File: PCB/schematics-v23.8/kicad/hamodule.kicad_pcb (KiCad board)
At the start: 2 copper layers, 129.2 x 84.3 mm, 146 parts, among them J1 GND|5V, J10 Tx|Rx, J11 USB_C_Receptacle_USB2.0, J12 2604-1104, J14 2604-1104, J15 2604-1104, J2 2604-1102, J3 Sda|Scl, J4 13|12, J5 9|3|16, J6 GND|3.3V, J7 Conn_01x02_Pin, J9 2604-1104, K1 AQG12205, K2 AQG12205, K3 AQG12205, K4 AQG12205, K5 AQG12205, K6 AQG12205, K7 AQG12205, K8 AQG12205, SW1 Reset, SW2 Boot, SW3 USB | PS, U1 LD1117AV33, U10 ULN2803A, U2 ESP32-S3-WROOM-2, U3 LDA210-PDIP, U4 USBLC6-2SC6, U5 LDA210-PDIP, U6 LDA210-PDIP, U7 SHT4x, U8 LDA210-PDIP, U9 MCP23017_SO

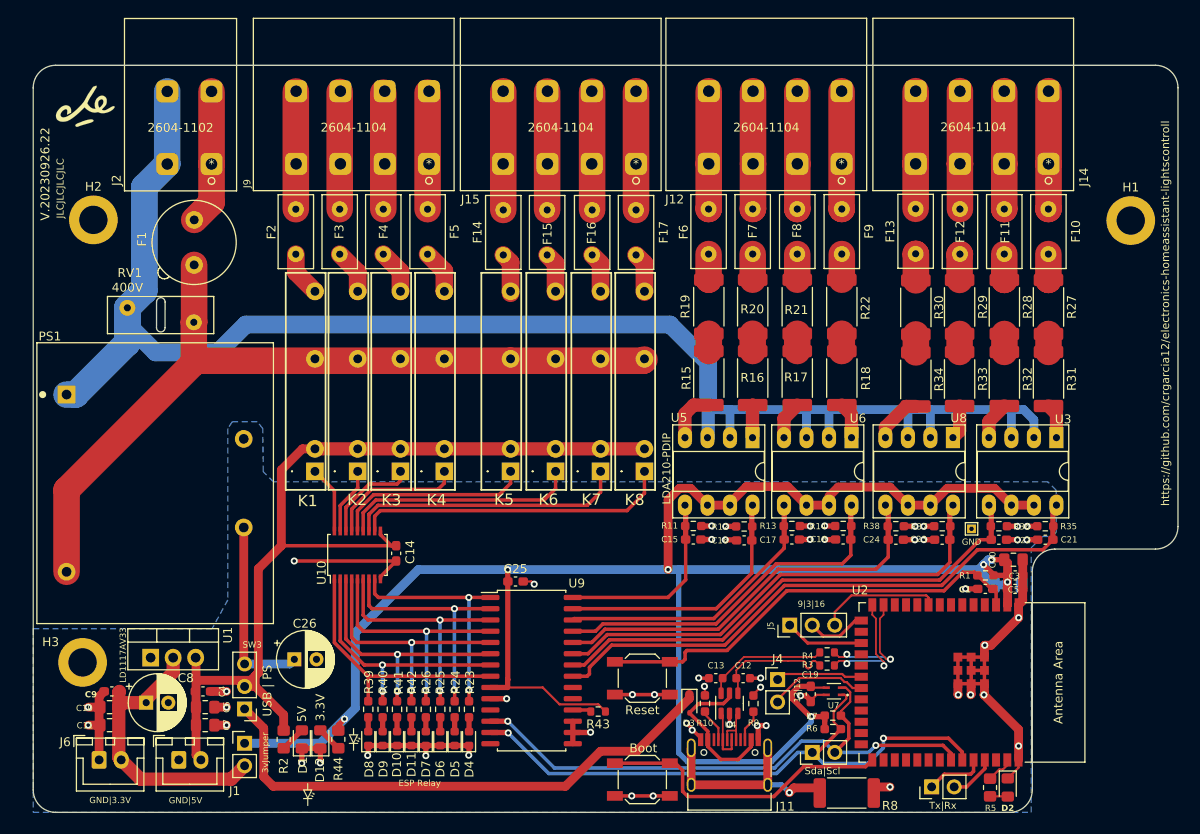
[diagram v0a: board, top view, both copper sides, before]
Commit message: [V23.8] Adding screen connector + Fixing version + adding caps
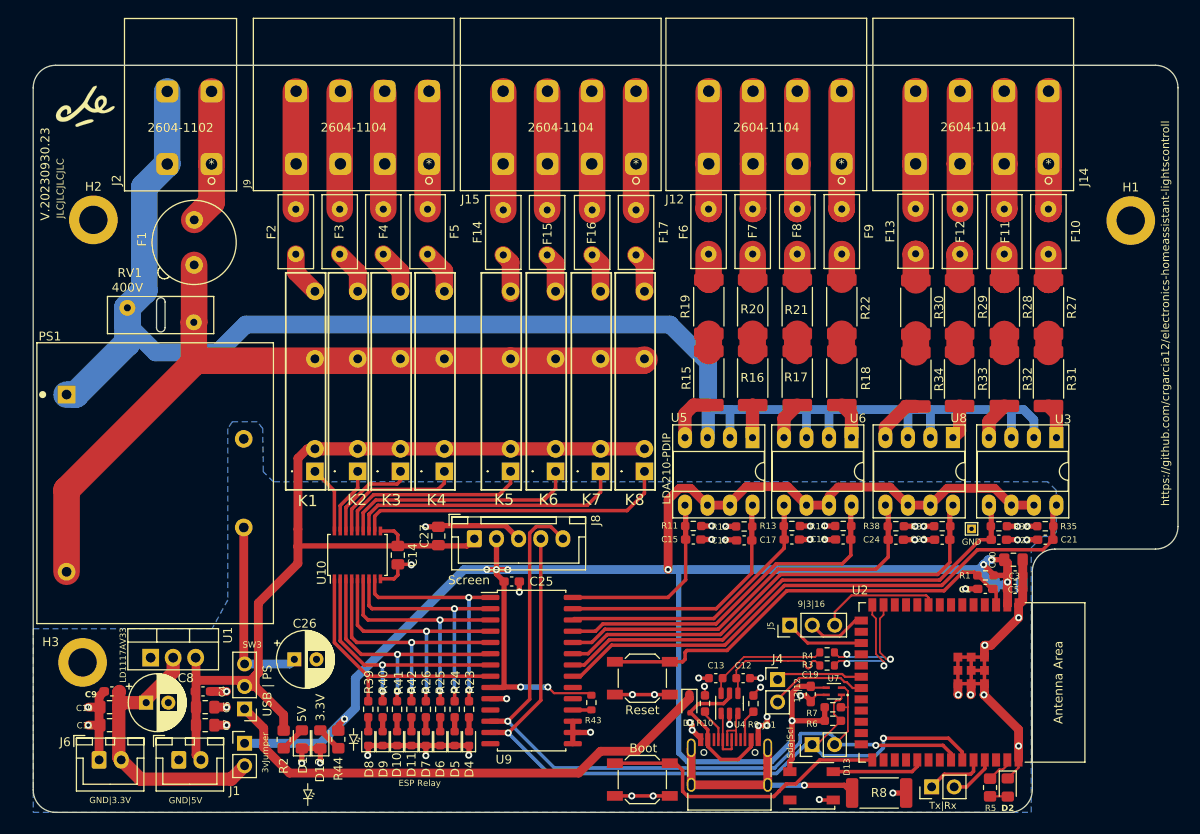
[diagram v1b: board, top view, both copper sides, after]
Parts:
- added C27: 22uF, Capacitor_SMD:C_0805_2012Metric_Pad1.18x1.45mm_HandSolder, F.Cu at (69.6, 85.3)
- added D13: Inolux_IN-PI554FCH, LED_SMD:LED_Inolux_IN-PI554FCH_PLCC4_5.0x5.0mm_P3.2mm, F.Cu at (111.7, 113.5)
- added J8: Screen, Connector_JST:JST_XH_B5B-XH-A_1x05_P2.50mm_Vertical, F.Cu at (73.7, 85.6)
- C14: footprint Capacitor_SMD:C_0603_1608Metric_Pad1.08x0.95mm_HandSolder -> Capacitor_SMD:C_0805_2012Metric_Pad1.18x1.45mm_HandSolder
- moved R8 3.66 mm to (119.4, 114.4)
- moved R43 1.27 mm to (86.9, 104.1), turned to -90 degrees
- moved R6 0.94 mm to (114.1, 106.2)
- moved R7 0.94 mm to (114.1, 104.7)
- moved J3 0.88 mm to (111.8, 108.9)
- moved C25 0.43 mm to (77.9, 90.5)
- moved C14 0.28 mm to (65.0, 87.5)
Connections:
- U2 pad 31: unconnected-(U2-GPIO38/FSPIWP/SUBSPIWP-Pad31) -> RGBLED
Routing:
- net SCL: track 68.3 -> 93.7 mm
- net SDA: track 69.6 -> 91.7 mm
- net RGBLED: track 0.00 -> 10.5 mm
- net 5V+: track 112.0 -> 119.7 mm
- net 3.3V+: track 246.2 -> 253.1 mm, vias 7 -> 11
- net GND: track 152.0 -> 155.5 mm, vias 52 -> 55
- net VBUS: track 61.6 -> 58.4 mm
- net Net-(J11-SHIELD): track 24.2 -> 26.9 mm
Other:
- board text added: "V.20230930.23"
- board text removed: "V.20230926.22"

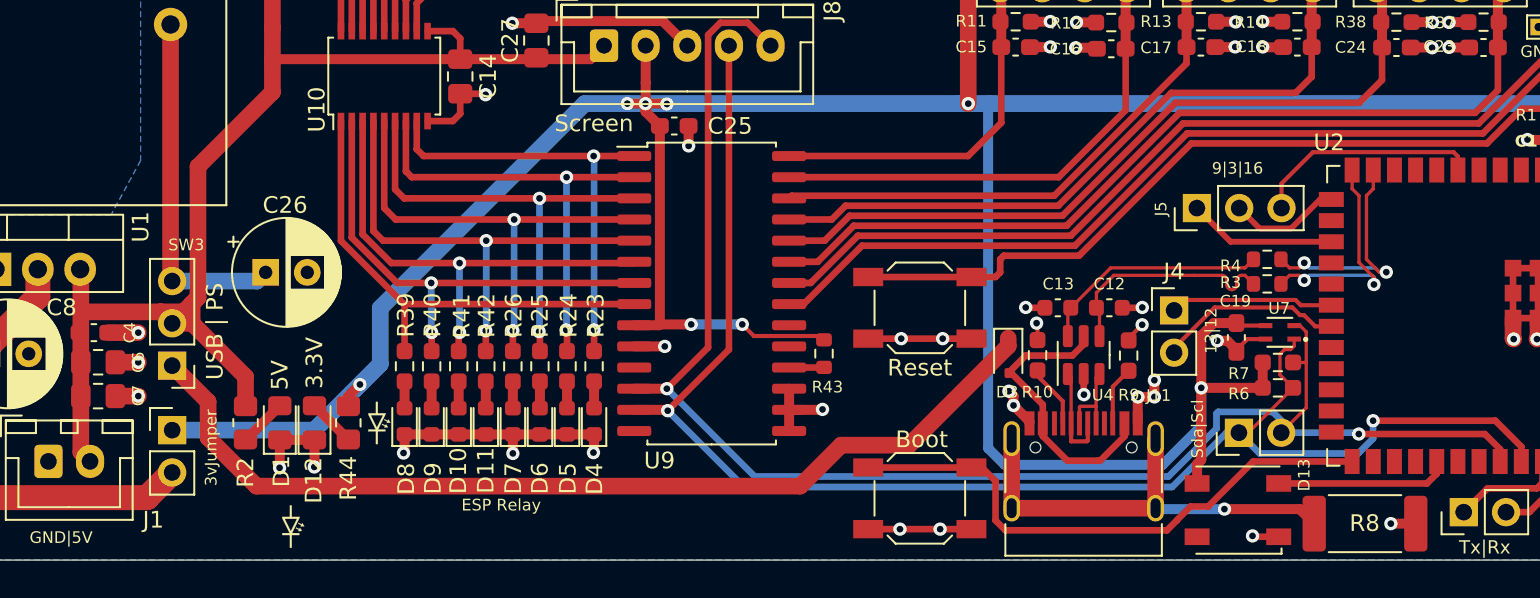
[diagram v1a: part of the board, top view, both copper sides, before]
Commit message: adding RGB Led
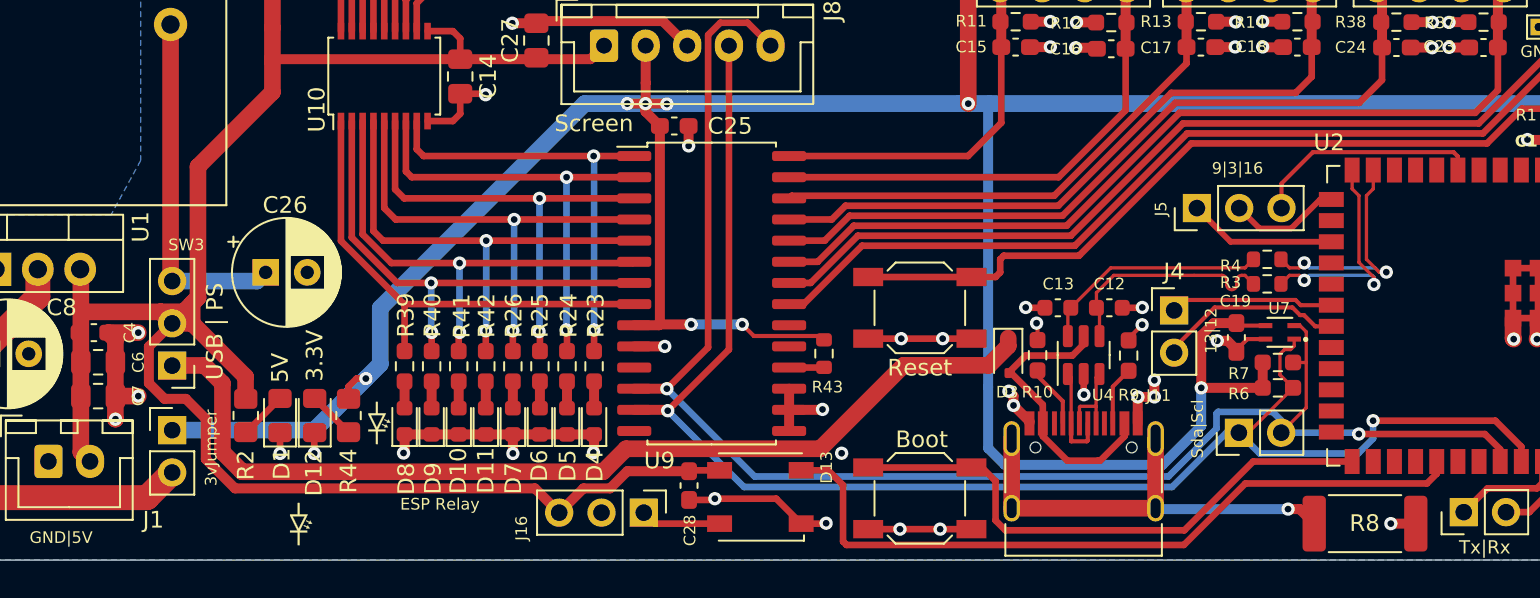
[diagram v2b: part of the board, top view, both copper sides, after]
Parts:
- added C28: 100nF, Capacitor_SMD:C_0603_1608Metric_Pad1.08x0.95mm_HandSolder, F.Cu at (78.8, 112.1)
- added J16: 9|3|16, Connector_PinHeader_2.54mm:PinHeader_1x03_P2.54mm_Vertical, F.Cu at (76.1, 113.7)
- moved D13 28.7 mm to (83.1, 112.8)
- moved G4 0.49 mm to (55.5, 114.4)
- moved D1 0.44 mm to (54.2, 107.9)
- moved D12 0.44 mm to (56.3, 107.9)
- moved R2 0.44 mm to (52.2, 107.9)
- moved R44 0.44 mm to (58.3, 107.9)
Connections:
- D13 pad 3: 3.3V+ -> 5V+
- D13 pad 4: unconnected-(D13-DO-Pad4) -> Net-(D13-DO)
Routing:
- net 5V+: track 119.7 -> 163.4 mm
- net RGBLED: track 10.5 -> 44.5 mm
- net GND: track 155.5 -> 163.9 mm, vias 55 -> 57
- net 3.3V+: track 253.1 -> 247.7 mm
- net Net-(D13-DO): track 0.00 -> 4.82 mm

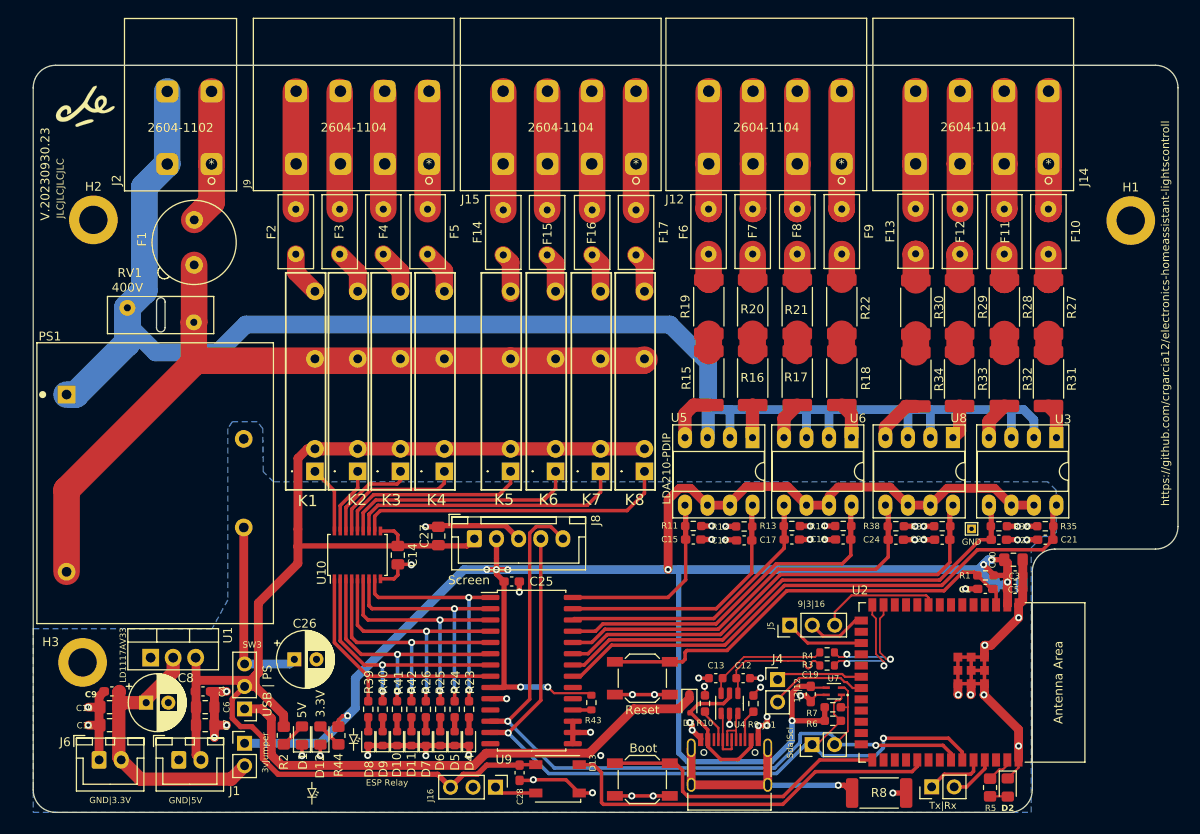
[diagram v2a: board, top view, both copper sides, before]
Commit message: [23.8] Adding RGB Led, fixing placing and silkscreen
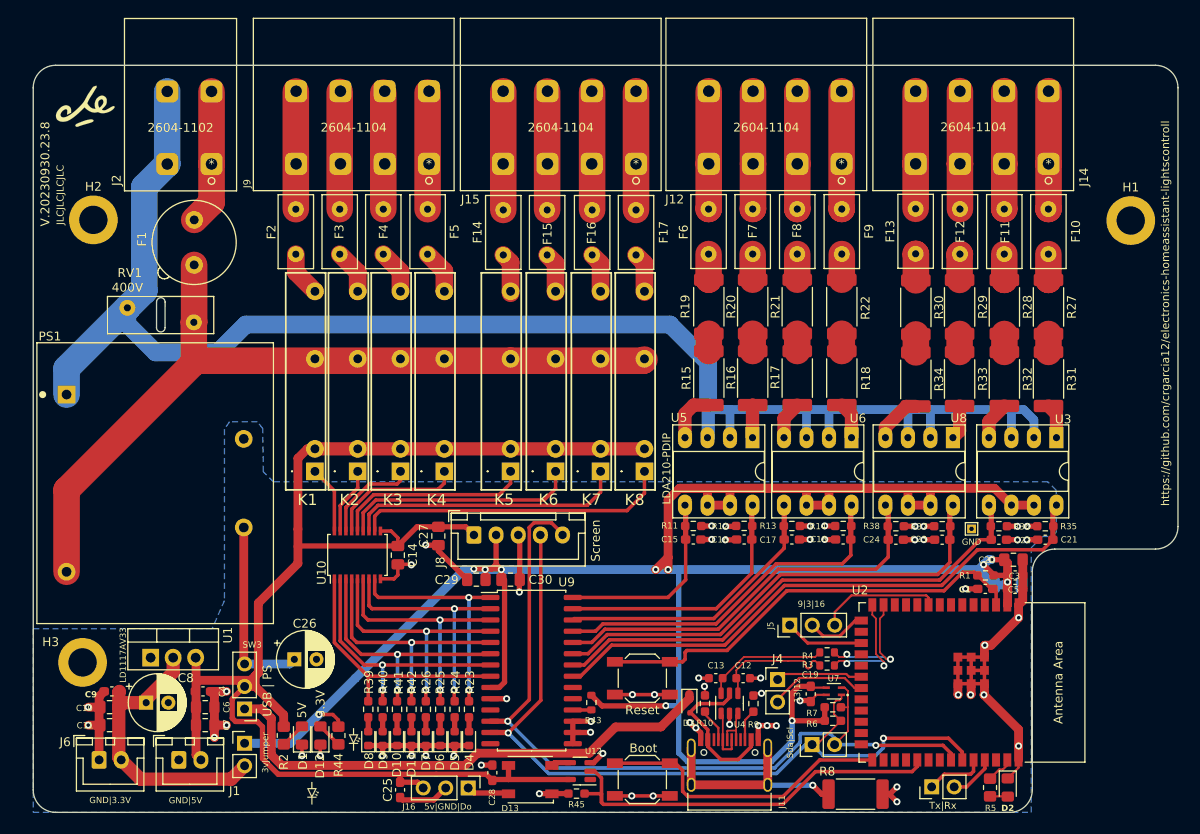
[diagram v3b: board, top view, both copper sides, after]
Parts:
- added C29: 100nF, Capacitor_SMD:C_0805_2012Metric_Pad1.18x1.45mm_HandSolder, F.Cu at (73.9, 90.3)
- added C30: 100nF, Capacitor_SMD:C_0805_2012Metric_Pad1.18x1.45mm_HandSolder, F.Cu at (77.8, 90.3)
- added R45: 10kΩ, Resistor_SMD:R_0603_1608Metric_Pad0.98x0.95mm_HandSolder, F.Cu at (85.2, 114.4)
- added U12: SN74LV1T34DBV, Package_TO_SOT_SMD:SOT-23-5, F.Cu at (85.6, 111.9)
- C27: value 22uF -> 100nF
- J16: value 9|3|16 -> 5v|GND|Do
- moved C25 26.7 mm to (65.3, 114.0), turned to -90 degrees
- moved D13 3.08 mm to (80.0, 112.8)
- moved J16 3.08 mm to (73.0, 113.8)
- moved C28 3.08 mm to (75.7, 112.1), turned to 90 degrees
- moved R8 2.67 mm to (116.7, 114.5)
- moved J8 0.43 mm to (73.6, 85.2)
- moved C16 0.10 mm to (104.1, 85.7)
- moved R12 0.06 mm to (104.1, 84.2)
- turned C27 to -90 degrees
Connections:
- C25 pad 1: 3.3V+ -> 5V+
- D13 pad 2: RGBLED -> Net-(D13-DIN)
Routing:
- net 3.3V+: track 247.7 -> 295.3 mm
- net GND: track 163.9 -> 173.3 mm, vias 57 -> 60
- net 5V+: track 163.4 -> 172.5 mm
- net Net-(J11-SHIELD): track 26.9 -> 24.3 mm
- net Net-(D13-DIN): track 0.00 -> 2.18 mm
- net RGBLED: track 44.5 -> 45.5 mm
- net SCL: track 93.7 -> 94.3 mm
- net 220VAC(N): track 111.3 -> 110.7 mm
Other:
- board text added: "V.20230930.23.8"
- board text removed: "ESP Relay"
- board text removed: "V.20230930.23"

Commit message: setting up for a new case
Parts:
- added G***: LOGO, icons:qr_code_m, B.Cu at (84.5, 104.4)
- moved G3 85.0 mm to (35.3, 78.4)
- moved G1 21.5 mm to (26.8, 58.1), turned to 90 degrees
- moved H2 14.1 mm to (27.0, 36.0)
- moved H1 14.0 mm to (150.3, 36.0)
- moved H3 10.6 mm to (27.0, 109.9)
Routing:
- net 3.3V+: track 295.3 -> 245.3 mm, vias 11 -> 7
- net GND: track 173.3 -> 211.3 mm, vias 60 -> 68
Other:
- board size 129.2 x 84.3 mm -> 129.6 x 84.3 mm
- board text added: "locked"
- board text removed: "JLCJLCJLCJLC"
- board text removed: "V.20230930.23.8"

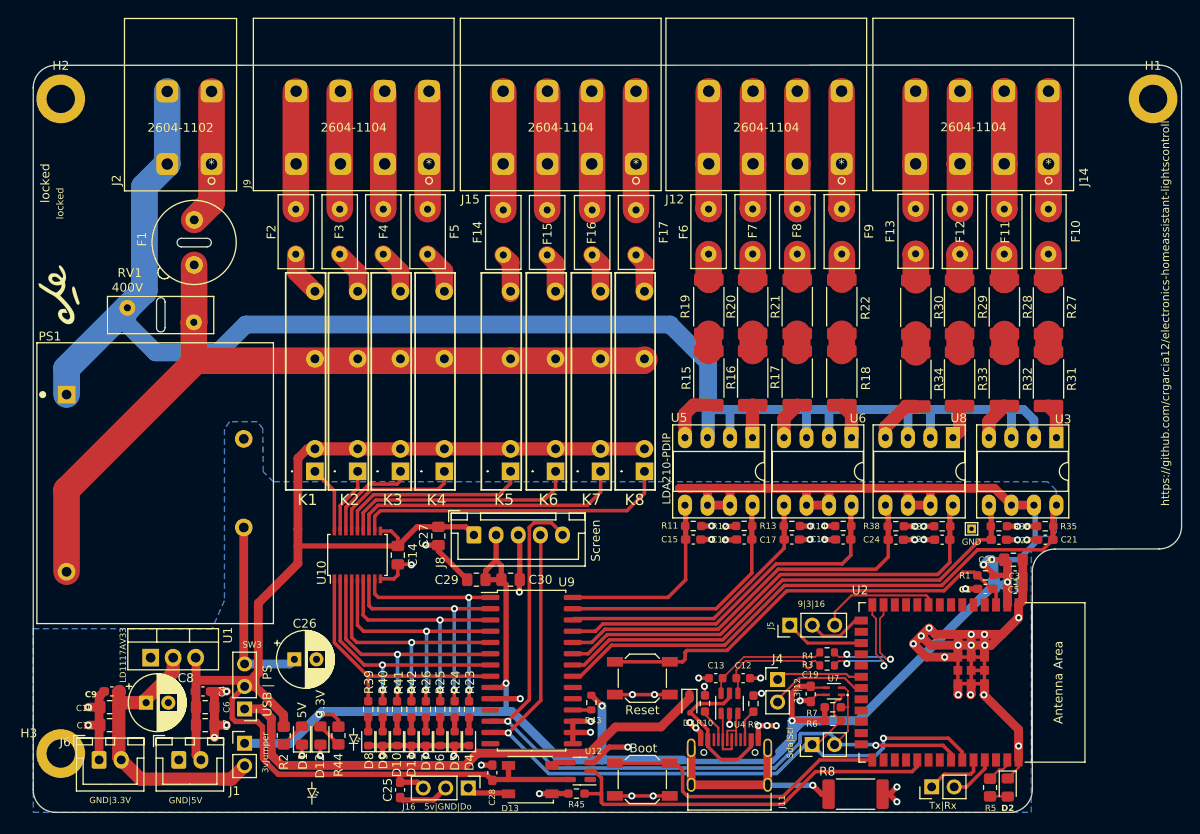
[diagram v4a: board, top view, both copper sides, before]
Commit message: fixing power sockets (3.3v and 5v) + prod files + readme
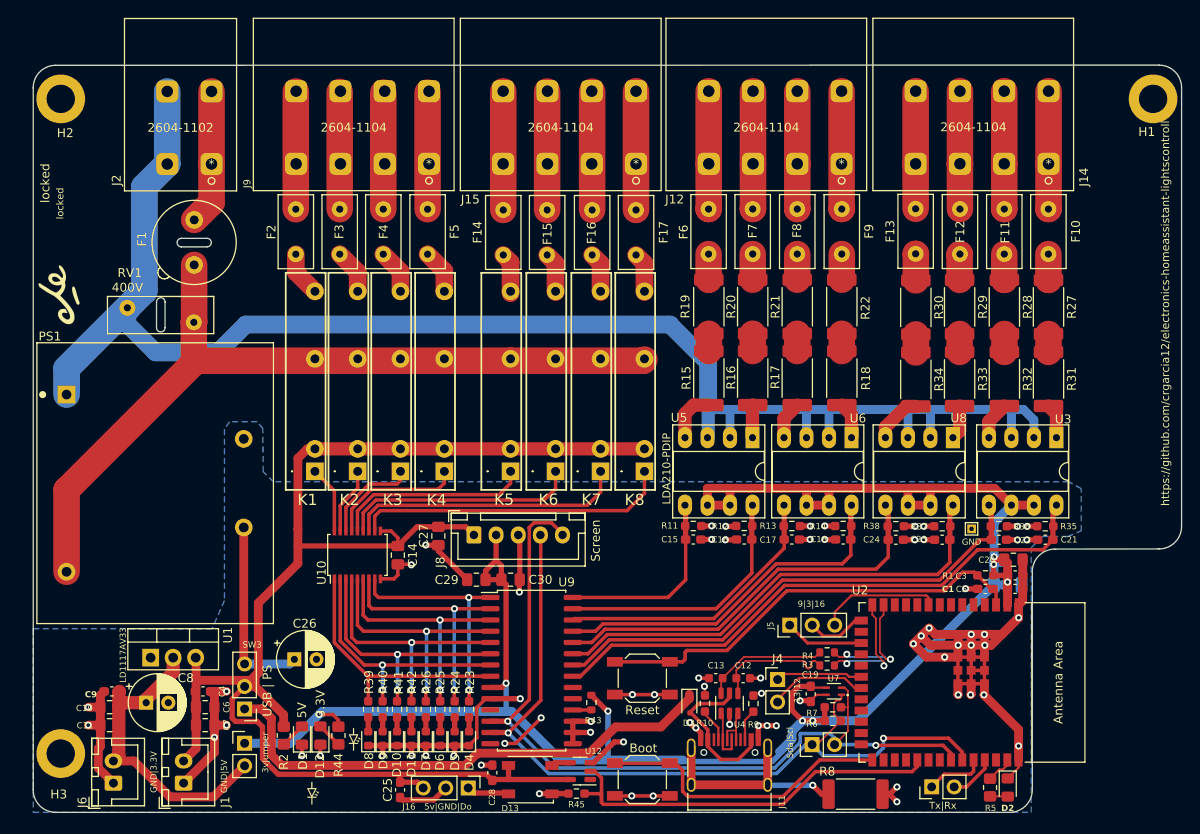
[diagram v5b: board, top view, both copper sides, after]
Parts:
- moved G3 102.6 mm to (136.4, 60.6)
- moved J6 3.08 mm to (32.9, 113.2), turned to 90 degrees
- moved J1 2.68 mm to (40.9, 113.2), turned to 90 degrees
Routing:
- net GND: track 211.3 -> 232.9 mm, vias 68 -> 70
- net 3.3V+: track 245.3 -> 236.3 mm, vias 7 -> 8
- net Net-(J6-Pin_2): track 33.0 -> 35.7 mm
